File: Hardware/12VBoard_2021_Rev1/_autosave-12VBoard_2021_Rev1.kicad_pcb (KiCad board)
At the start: 2 copper layers, 178 parts, among them Q1 CSD18537NQ5A, Q2 CSD18531Q5A, Q3 IRFZ34, Q4 CSD18537NQ5A, Q5 CSD18531Q5A, Q6 CSD18537NQ5A, Q7 CSD18531Q5A, SW1 SW_SPDT, U1 LM2576SX-5.0/NOPB, U10 LM5116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

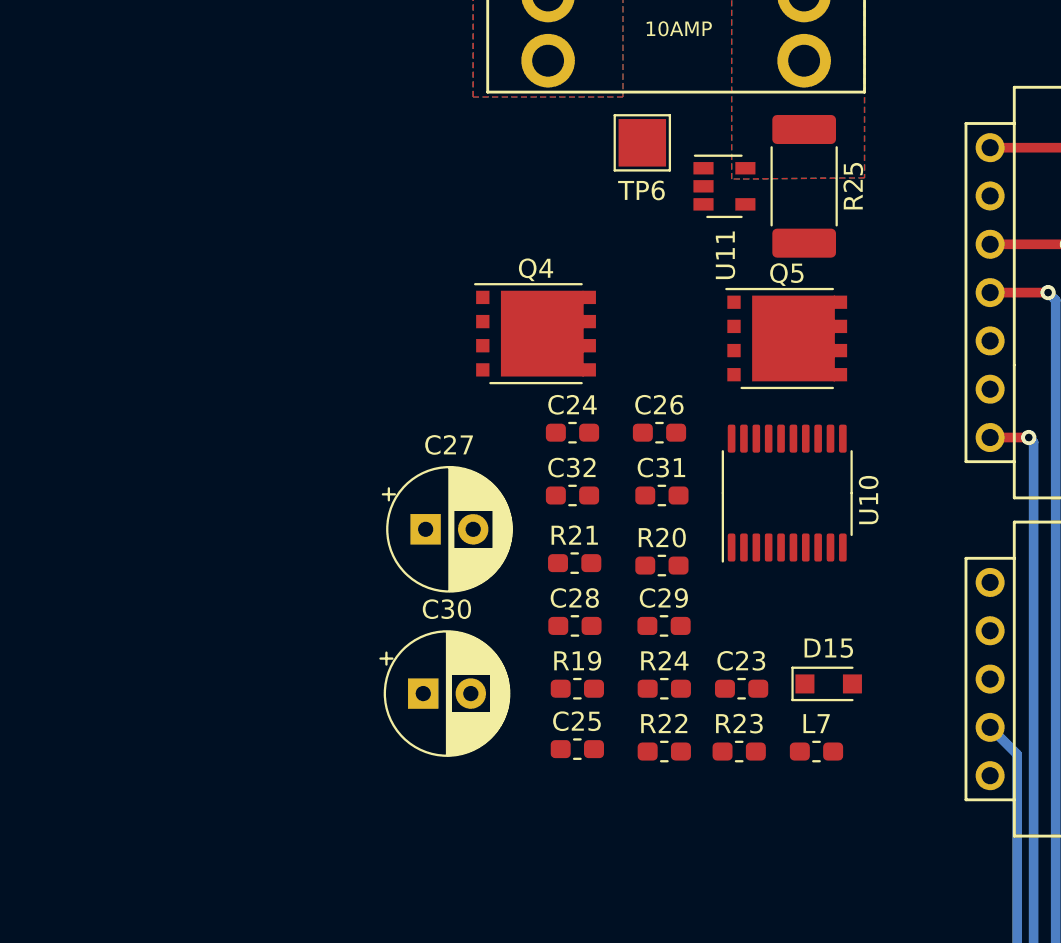
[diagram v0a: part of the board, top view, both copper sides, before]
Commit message: Started High Current Tracing
(Crash happened)
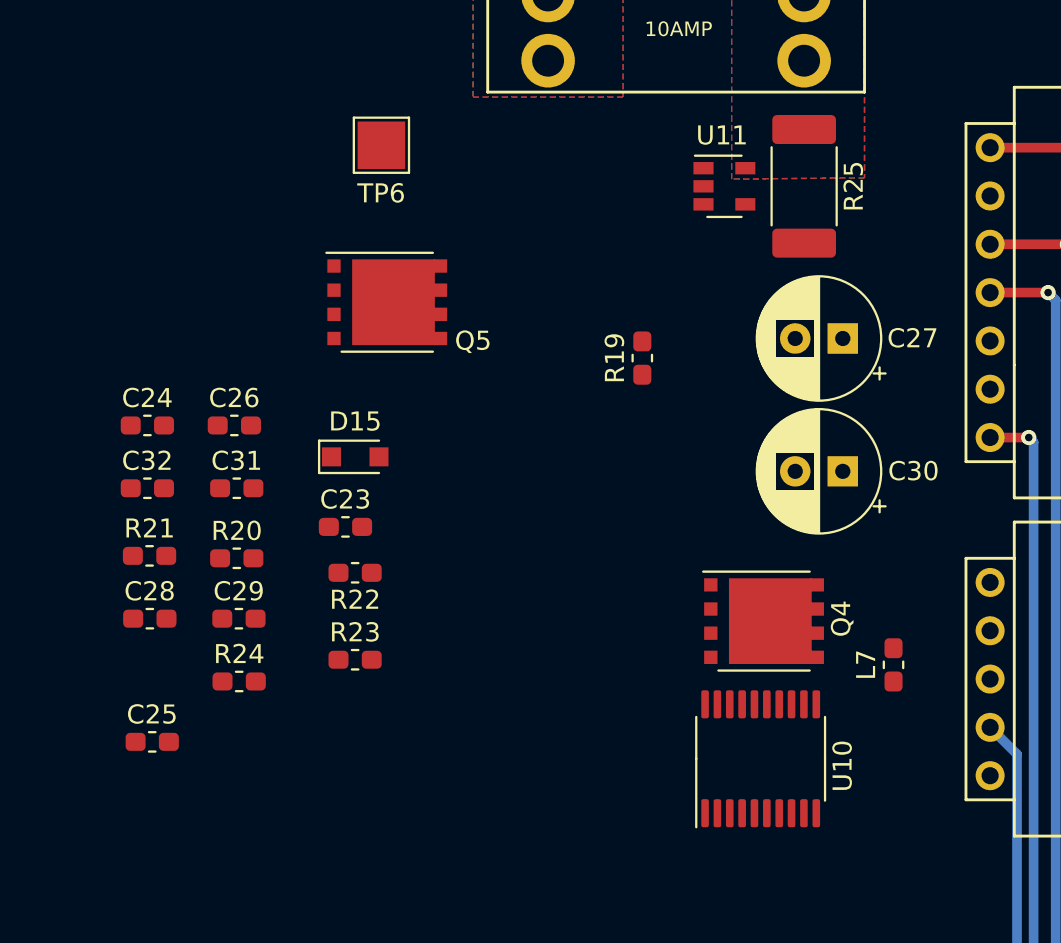
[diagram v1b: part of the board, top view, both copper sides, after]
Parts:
- moved D15 27.6 mm to (181.2, 70.9)
- moved C30 25.0 mm to (206.9, 71.6), turned to 180 degrees
- moved C27 24.1 mm to (206.9, 64.6), turned to 180 degrees
- moved C23 22.5 mm to (180.7, 74.5)
- moved C24 22.4 mm to (170.3, 69.2)
- moved C25 22.4 mm to (170.6, 85.9)
- moved C26 22.4 mm to (174.9, 69.2)
- moved C28 22.4 mm to (170.4, 79.4)
- moved C29 22.4 mm to (175.1, 79.4)
- moved C31 22.4 mm to (175.0, 72.5)
- moved C32 22.4 mm to (170.3, 72.5)
- moved R20 22.4 mm to (175.0, 76.2)
- moved R21 22.4 mm to (170.4, 76.1)
- moved R24 22.4 mm to (175.1, 82.7)
- moved Q5 21.1 mm to (182.9, 62.7)
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
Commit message: packVoltage line not connected in schematic
Sheet pins were used instead of hierarchical pins, which caused the line to not be continuous. Now it is connected
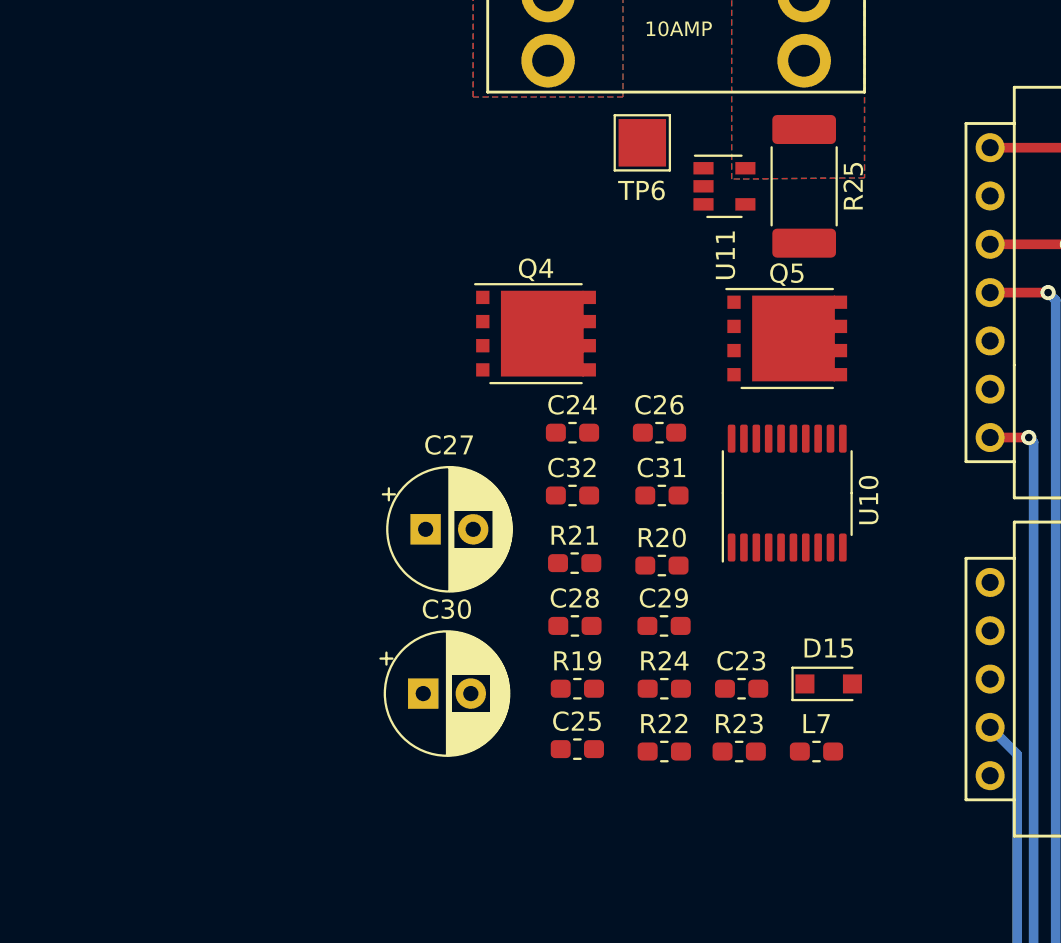
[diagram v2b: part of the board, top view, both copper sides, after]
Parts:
- moved D15 27.6 mm to (206.1, 82.8)
- moved C30 25.0 mm to (184.8, 83.3), turned to 0 degrees
- moved C27 24.1 mm to (185.0, 74.7), turned to 0 degrees
- moved C23 22.5 mm to (201.6, 83.1)
- moved C24 22.4 mm to (192.7, 69.6)
- moved C25 22.4 mm to (192.9, 86.2)
- moved C26 22.4 mm to (197.2, 69.6)
- moved C28 22.4 mm to (192.8, 79.8)
- moved C29 22.4 mm to (197.5, 79.8)
- moved C31 22.4 mm to (197.4, 72.9)
- moved C32 22.4 mm to (192.7, 72.9)
- moved R20 22.4 mm to (197.4, 76.6)
- moved R21 22.4 mm to (192.8, 76.5)
- moved R24 22.4 mm to (197.5, 83.1)
- moved Q5 21.1 mm to (204.0, 64.6)
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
